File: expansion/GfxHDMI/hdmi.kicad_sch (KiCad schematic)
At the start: 16 parts, among them J4 685119134923

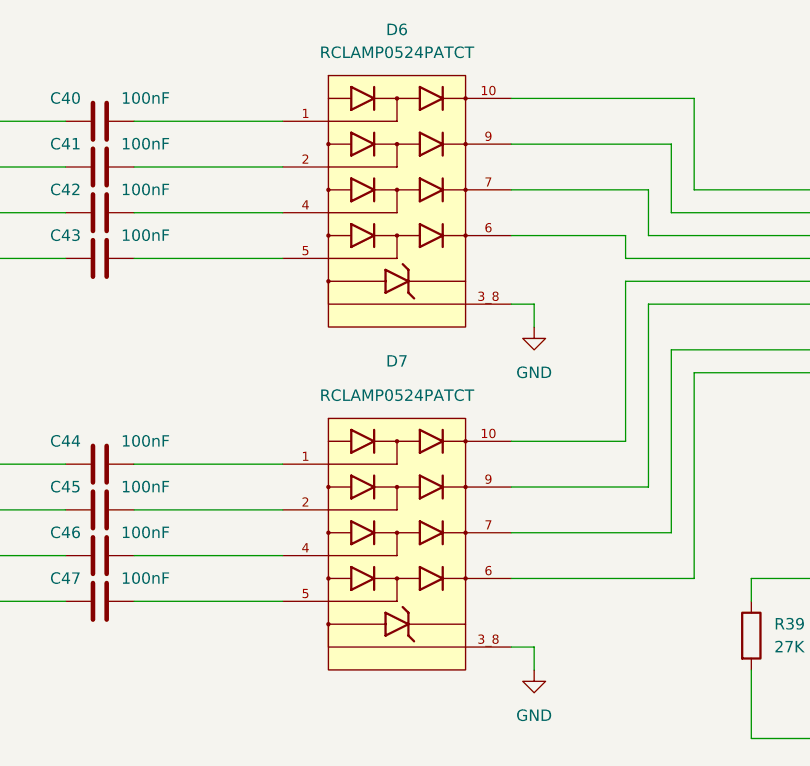
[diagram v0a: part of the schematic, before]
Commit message: Changes to the HDMI board
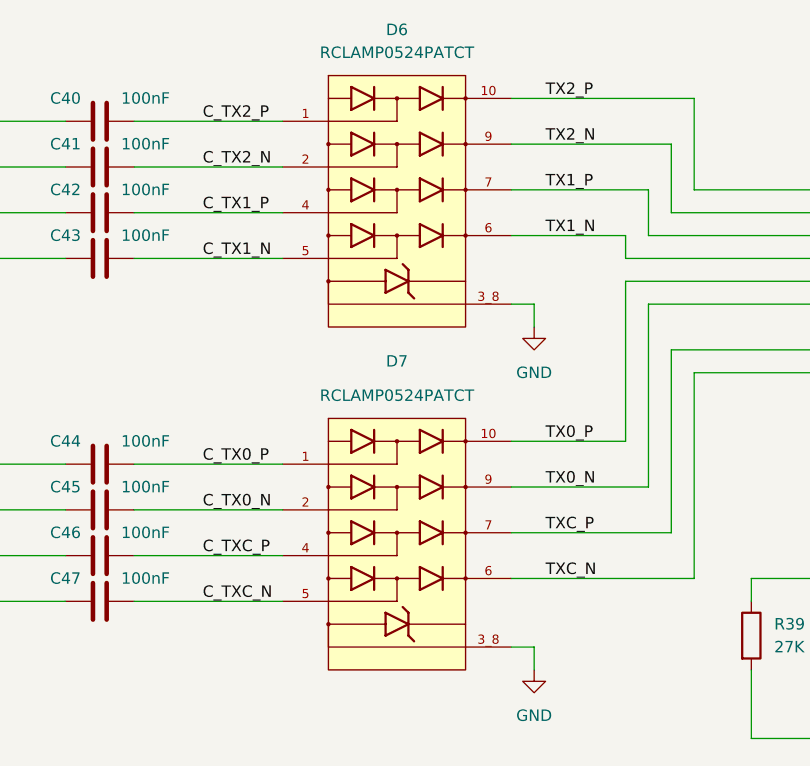
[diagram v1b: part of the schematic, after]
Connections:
- net C_TX2_P: now reaches C40.2, D6.1
- net TX2_P: now reaches D6.10, J4.1 (DATA2+)
- net C_TX2_N: now reaches C41.2, D6.2
- net C_TX1_P: now reaches C42.2, D6.4
- net C_TX1_N: now reaches C43.2, D6.5
- net TX1_N: now reaches D6.6, J4.6 (DATA1-)
- net TX1_P: now reaches D6.7, J4.4 (DATA1+)
- net TX2_N: now reaches D6.9, J4.3 (DATA2-)
- net C_TXC_P: now reaches C46.2, D7.4
- net C_TX0_P: now reaches C44.2, D7.1
- net C_TX0_N: now reaches C45.2, D7.2
- net TX0_P: now reaches D7.10, J4.7 (DATA0+)
- net C_TXC_N: now reaches C47.2, D7.5
- net TXC_N: now reaches D7.6, J4.12 (CLOCK-)
- net TXC_P: now reaches D7.7, J4.10 (CLOCK+)
- net TX0_N: now reaches D7.9, J4.9 (DATA0-)
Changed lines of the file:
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@@
+		)
+	)
+	(label "C_TX0_N"
+		(at 113.03 99.06 0)
+		(fields_autoplaced yes)
+		(effects
+			(font
+				(size 1.27 1.27)
+			)
+			(justify left bottom)
 		)
 	)
@@
 		)
 	)
+	(label "TX1_N"
+		(at 151.13 68.58 0)
+		(fields_autoplaced yes)
+		(effects
+			(font
+				(size 1.27 1.27)
+			)
+			(justify left bottom)
+		)
+	)
+	(label "TX0_N"
+		(at 151.13 96.52 0)
+		(fields_autoplaced yes)
+		(effects
+			(font
+				(size 1.27 1.27)
+			)
+			(justify left bottom)
+		)
+	)
+	(label "C_TX0_P"
+		(at 113.03 93.98 0)
+		(fields_autoplaced yes)
+		(effects
+			(font
+				(size 1.27 1.27)
+			)
+			(justify left bottom)
+		)
+	)
+	(label "C_TXC_P"
+		(at 113.03 104.14 0)
+		(fields_autoplaced yes)
+		(effects
+			(font
+				(size 1.27 1.27)
+			)
+			(justify left bottom)
+		)
+	)
 	(label "HDMI_TX2_N"
 		(at 87.63 60.96 180)
@@
 		)
 	)
+	(label "TX1_P"
+		(at 151.13 63.5 0)
+		(fields_autoplaced yes)
+		(effects
+			(font
+				(size 1.27 1.27)
+			)
+			(justify left bottom)
+		)
+	)
+	(label "TX2_P"
+		(at 151.13 53.34 0)
+		(fields_autoplaced yes)
+		(effects
+			(font
+				(size 1.27 1.27)
+			)
+			(justify left bottom)
+		)
+	)
+	(label "C_TX2_P"
+		(at 113.03 55.88 0)
+		(fields_autoplaced yes)
+		(effects
+			(font
+				(size 1.27 1.27)
+			)
+			(justify left bottom)
+		)
+	)
+	(label "TXC_N"
+		(at 151.13 106.68 0)
+		(fields_autoplaced yes)
+		(effects
+			(font
+				(size 1.27 1.27)
+			)
+			(justify left bottom)
+		)
+	)
+	(label "TX2_N"
+		(at 151.13 58.42 0)
+		(fields_autoplaced yes)
+		(effects
+			(font
+				(size 1.27 1.27)
+			)
+			(justify left bottom)
+		)
+	)
+	(label "TXC_P"
+		(at 151.13 101.6 0)
+		(fields_autoplaced yes)
+		(effects
+			(font
+				(size 1.27 1.27)
+			)
+			(justify left bottom)
+		)
+	)
+	(label "C_TX1_N"
+		(at 113.03 71.12 0)
+		(fields_autoplaced yes)
+		(effects
+			(font
+				(size 1.27 1.27)
+			)
+			(justify left bottom)
+		)
+	)
+	(label "C_TX1_P"
+		(at 113.03 66.04 0)
+		(fields_autoplaced yes)
+		(effects
+			(font
+				(size 1.27 1.27)
+			)
+			(justify left bottom)
+		)
+	)
+	(label "C_TXC_N"
+		(at 113.03 109.22 0)
+		(fields_autoplaced yes)
+		(effects
+			(font
+				(size 1.27 1.27)
+			)
+			(justify left bottom)
+		)
+	)
+	(label "TX0_P"
+		(at 151.13 91.44 0)
+		(fields_autoplaced yes)
+		(effects
+			(font
+				(size 1.27 1.27)
+			)
+			(justify left bottom)
+		)
+	)
 	(label "HDMI_TX0_N"
 		(at 87.63 99.06 180)
@@
 		)
 	)
+	(label "C_TX2_N"
+		(at 113.03 60.96 0)
+		(fields_autoplaced yes)
+		(effects
+			(font
+				(size 1.27 1.27)
+			)
+			(justify left bottom)
+		)
+	)
